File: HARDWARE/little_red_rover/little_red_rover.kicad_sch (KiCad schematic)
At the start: 49 parts, among them J1 USB_C_Receptacle_USB2.0_14P, J2 Conn_01x04_Socket, J3 Conn_01x02_Socket, J4 Conn_01x02_Socket, J5 Conn_01x01_Socket, J6 Conn_01x01_Socket, U1 ESP32-C3-MINI-1, U2 BQ24230RGT, U3 MIC5504-3.3YM5, U4 TPS613222ADBV, U5 DRV8212P, U6 DRV8212P, U7 GP1S094HCZ0F, U8 GP1S094HCZ0F, U9 LSM6DS3

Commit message: Update schematic: use ESP32-S3 mini, unflip usb lines, fix charger CE polarity, add header pins for GPIO, add buttons for strapping pins
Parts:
- removed U1: ESP32-C3-MINI-1, Espressif:ESP32-C3-MINI-1_HandSoldering, symbol Espressif:ESP32-C3-MINI-1
- added C13, C14, C15: 0.1uF, symbol Device:C
- added C6: 1uF, symbol Device:C
- added J7: Conn_02x10_Odd_Even, symbol Connector_Generic:Conn_02x10_Odd_Even
- added R16, R17, R9: 10k, symbol Device:R
- added SW1, SW2, SW3: SW_Push, symbol Switch:SW_Push
- added U10: ESP32-S3-MINI-1, PCM_Espressif:ESP32-S3-MINI-1, symbol Espressif:ESP32-S3-MINI-1
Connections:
- net +3.3V: now also R16.1, R17.1, R9.1, U10.3 (3V3)
- net GND: now also U2.4 (CE), C13.1, C14.1, C15.1, C6.2, SW1.1, SW2.1, SW3.1, U10.1 (GND), U10.2 (GND), U10.41 (GPIO45), U10.42 (GND), U10.43 (GND), U10.44 (GPIO46), U10.46 (GND), U10.47 (GND), U10.48 (GND), U10.49 (GND), U10.50 (GND), U10.51 (GND), U10.52 (GND), U10.53 (GND), U10.54 (GND), U10.55 (GND), U10.56 (GND), U10.57 (GND), U10.58 (GND), U10.59 (GND), U10.60 (GND), U10.61 (GND), U10.62 (GND), U10.63 (GND), U10.64 (GND), U10.65 (GND)
- net charger_out: no longer U2.4 (CE)
- net imu_scl: now also U10.5 (GPIO1/TOUCH1/ADC1_CH0)
- net imu_sda: now also U10.6 (GPIO2/TOUCH2/ADC1_CH1)
- net left_encoder: now also U10.8 (GPIO4/TOUCH4/ADC1_CH3)
- net left_motor_pwm_a: now also U10.10 (GPIO6/TOUCH6/ADC1_CH5)
- net left_motor_pwm_b: now also U10.11 (GPIO7/TOUCH7/ADC1_CH6)
- net lidar_tx: now also U10.22 (GPIO18/U1RXD/ADC2_CH7/CLK_OUT3)
- net motor_sleep: now also R17.2, U10.9 (GPIO5/TOUCH5/ADC1_CH4)
- net right_encoder: now also U10.7 (GPIO3/TOUCH3/ADC1_CH2)
- net right_motor_pwm_a: now also U10.12 (GPIO8/TOUCH8/ADC1_CH7/SUBSPICS1)
- net right_motor_pwm_b: now also U10.13 (GPIO9/TOUCH9/ADC1_CH8/FSPIHD/SUBSPIHD)
- net status_leds: now also U10.14 (GPIO10/TOUCH10/ADC1_CH9/FSPICS0/FSPIIO4/SUBSPICS0)
- net usb_data_+: now also J1.A6 (D+), J1.B6 (D+), U10.24 (GPIO20/U1CTS/ADC2_CH9/CLK_OUT1/USB_D+); no longer J1.A7 (D-), J1.B7 (D-)
- net usb_data_-: now also J1.A7 (D-), J1.B7 (D-), U10.23 (GPIO19/U1RTS/ADC2_CH8/CLK_OUT2/USB_D-); no longer J1.A6 (D+), J1.B6 (D+)
- new net GPIO_12: J7.1 (Pin_1), U10.16 (GPIO12/TOUCH12/ADC2_CH1/FSPICLK/FSPIIO6/SUBSPICLK)
- new net GPIO_13: J7.2 (Pin_2), U10.17 (GPIO13/TOUCH13/ADC2_CH2/FSPIQ/FSPIIO7/SUBSPIQ)
- new net GPIO_14: J7.3 (Pin_3), U10.18 (GPIO14/TOUCH14/ADC2_CH3/FSPIWP/FSPIDQS/SUBSPIWP)
- new net GPIO_15: J7.4 (Pin_4), U10.19 (GPIO15/U0RTS/ADC2_CH4/XTAL_32K_P)
- new net GPIO_16: J7.5 (Pin_5), U10.20 (GPIO16/U0CTS/ADC2_CH5/XTAL_32K_N)
- new net GPIO_21: J7.6 (Pin_6), U10.25 (GPIO21)
- new net GPIO_33: J7.7 (Pin_7), U10.28 (SPIIO4/GPIO33/FSPIHD/SUBSPIHD)
- new net GPIO_34: J7.8 (Pin_8), U10.29 (SPIIO5/GPIO34/FSPICS0/SUBSPICS0)
- new net GPIO_35: J7.9 (Pin_9), U10.31 (SPIIO6/GPIO35/FSPID/SUBSPID)
- new net GPIO_36: J7.10 (Pin_10), U10.32 (SPIIO7/GPIO36/FSPICLK/SUBSPICLK)
- new net GPIO_37: J7.11 (Pin_11), U10.33 (SPIDQS/GPIO37/FSPIQ/SUBSPIQ)
- new net GPIO_38: J7.12 (Pin_12), U10.34 (GPIO38/FSPIWP/SUBSPIWP)
- new net GPIO_39: J7.13 (Pin_13), U10.35 (MTCK/GPIO39/CLK_OUT3/SUBSPICS1)
- new net GPIO_40: J7.14 (Pin_14), U10.36 (MTDO/GPIO40/CLK_OUT2)
- new net GPIO_41: J7.15 (Pin_15), U10.37 (MTDI/GPIO41/CLK_OUT1)
- new net GPIO_42: J7.16 (Pin_16), U10.38 (MTMS/GPIO42)
- new net GPIO_43: J7.17 (Pin_17), U10.39 (U0TXD/GPIO43/CLK_OUT1)
- new net GPIO_44: J7.18 (Pin_18), U10.40 (U0RXD/GPIO44/CLK_OUT2)
- new net GPIO_47: J7.19 (Pin_19), U10.27 (GPIO47/SPICLK_P/SUBSPICLK_P_DIFF)
- new net GPIO_48: J7.20 (Pin_20), U10.30 (GPIO48/SPICLK_N/SUBSPICLK_N_DIFF)
- new net boot: C13.2, SW1.2, U10.4 (GPIO0/BOOT)
- new net chip_en: C14.2, C6.1, R9.2, SW2.2, U10.45 (EN)
- new net reprovision: C15.2, R16.2, SW3.2, U10.15 (GPIO11/TOUCH11/ADC2_CH0/FSPID/FSPIIO5/SUBSPID)
- no-connect marks 4 -> 7
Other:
- note added: "headers"
- note added: "pin strapping"
- moved on the sheet: C1, C10, C11, C12, C2, C3, C4, C5, C7, C8, C9, D1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

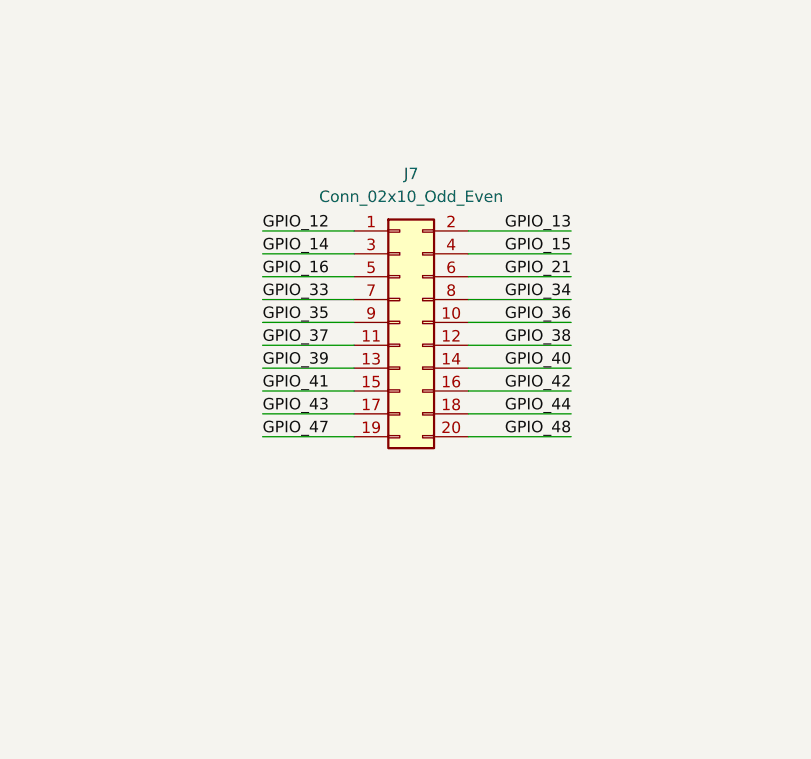
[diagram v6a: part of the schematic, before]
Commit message: Update PCB layout: Position components for new schematic updates
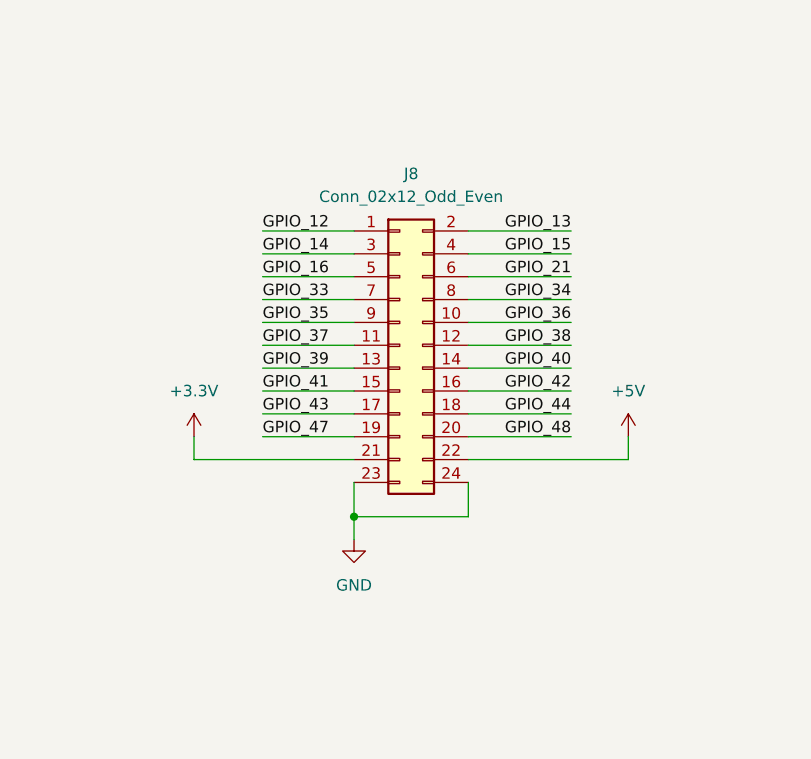
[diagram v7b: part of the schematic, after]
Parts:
- removed J7: Conn_02x10_Odd_Even, symbol Connector_Generic:Conn_02x10_Odd_Even
- added J8: Conn_02x12_Odd_Even, Connector_PinHeader_2.54mm:PinHeader_2x12_P2.54mm_Vertical, symbol Connector_Generic:Conn_02x12_Odd_Even
- C13, C14, C15, C6: footprint (none) -> Capacitor_SMD:C_0603_1608Metric_Pad1.08x0.95mm_HandSolder
- R16, R17, R9: footprint (none) -> Resistor_SMD:R_0603_1608Metric_Pad0.98x0.95mm_HandSolder
- SW1, SW2, SW3: footprint (none) -> Button_Switch_SMD:SW_Tactile_SPST_NO_Straight_CK_PTS636Sx25SMTRLFS
- U10: footprint PCM_Espressif:ESP32-S3-MINI-1 -> Espressif:ESP32-S2-MINI-1_HandSoldering
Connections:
- net +3.3V: now also J8.21 (Pin_21)
- net +5V: now also J8.22 (Pin_22)
- net GND: now also J8.23 (Pin_23), J8.24 (Pin_24)
- net GPIO_12: now also J8.1 (Pin_1)
- net GPIO_13: now also J8.2 (Pin_2)
- net GPIO_14: now also J8.3 (Pin_3)
- net GPIO_15: now also J8.4 (Pin_4)
- net GPIO_16: now also J8.5 (Pin_5)
- net GPIO_21: now also J8.6 (Pin_6)
- net GPIO_33: now also J8.7 (Pin_7)
- net GPIO_34: now also J8.8 (Pin_8)
- net GPIO_35: now also J8.9 (Pin_9)
- net GPIO_36: now also J8.10 (Pin_10)
- net GPIO_37: now also J8.11 (Pin_11)
- net GPIO_38: now also J8.12 (Pin_12)
- net GPIO_39: now also J8.13 (Pin_13)
- net GPIO_40: now also J8.14 (Pin_14)
- net GPIO_41: now also J8.15 (Pin_15)
- net GPIO_42: now also J8.16 (Pin_16)
- net GPIO_43: now also J8.17 (Pin_17)
- net GPIO_44: now also J8.18 (Pin_18)
- net GPIO_47: now also J8.19 (Pin_19)
- net GPIO_48: now also J8.20 (Pin_20)

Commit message: Route traces for v1.1
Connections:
- net +3.3V: now also J8.20 (Pin_20), J8.22 (Pin_22); no longer J2.1 (Pin_1), J8.21 (Pin_21)
- net +5V: now also J8.21 (Pin_21); no longer J8.22 (Pin_22)
- net GPIO_12: now also J8.2 (Pin_2); no longer J8.1 (Pin_1)
- net GPIO_13: now also J8.1 (Pin_1); no longer J8.2 (Pin_2)
- net GPIO_14: now also J8.4 (Pin_4); no longer J8.3 (Pin_3)
- net GPIO_15: now also J8.3 (Pin_3); no longer J8.4 (Pin_4)
- net GPIO_16: now also J8.6 (Pin_6); no longer J8.5 (Pin_5)
- net GPIO_21: now also J8.5 (Pin_5); no longer J8.6 (Pin_6)
- net GPIO_33: now also J8.8 (Pin_8); no longer J8.7 (Pin_7)
- net GPIO_34: now also J8.7 (Pin_7); no longer J8.8 (Pin_8)
- net GPIO_35: now also J8.10 (Pin_10); no longer J8.9 (Pin_9)
- net GPIO_36: now also J8.9 (Pin_9); no longer J8.10 (Pin_10)
- net GPIO_37: now also J8.12 (Pin_12); no longer J8.11 (Pin_11)
- net GPIO_38: now also J8.11 (Pin_11); no longer J8.12 (Pin_12)
- net GPIO_39: now also J8.14 (Pin_14); no longer J8.13 (Pin_13)
- net GPIO_40: now also J8.13 (Pin_13); no longer J8.14 (Pin_14)
- net GPIO_41: now also J8.16 (Pin_16); no longer J8.15 (Pin_15)
- net GPIO_42: now also J8.15 (Pin_15); no longer J8.16 (Pin_16)
- net GPIO_43: now also J8.18 (Pin_18); no longer J8.17 (Pin_17)
- net GPIO_44: now also J8.17 (Pin_17); no longer J8.18 (Pin_18)
- net GPIO_48: now also J8.19 (Pin_19); no longer J8.20 (Pin_20)
- net GPIO_47 renamed lidar_pwm
- net lidar_pwm: now also J2.1 (Pin_1); no longer J8.19 (Pin_19)
